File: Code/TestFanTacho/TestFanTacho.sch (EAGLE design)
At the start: 10 parts, among them IC1 317T, T1 BC548

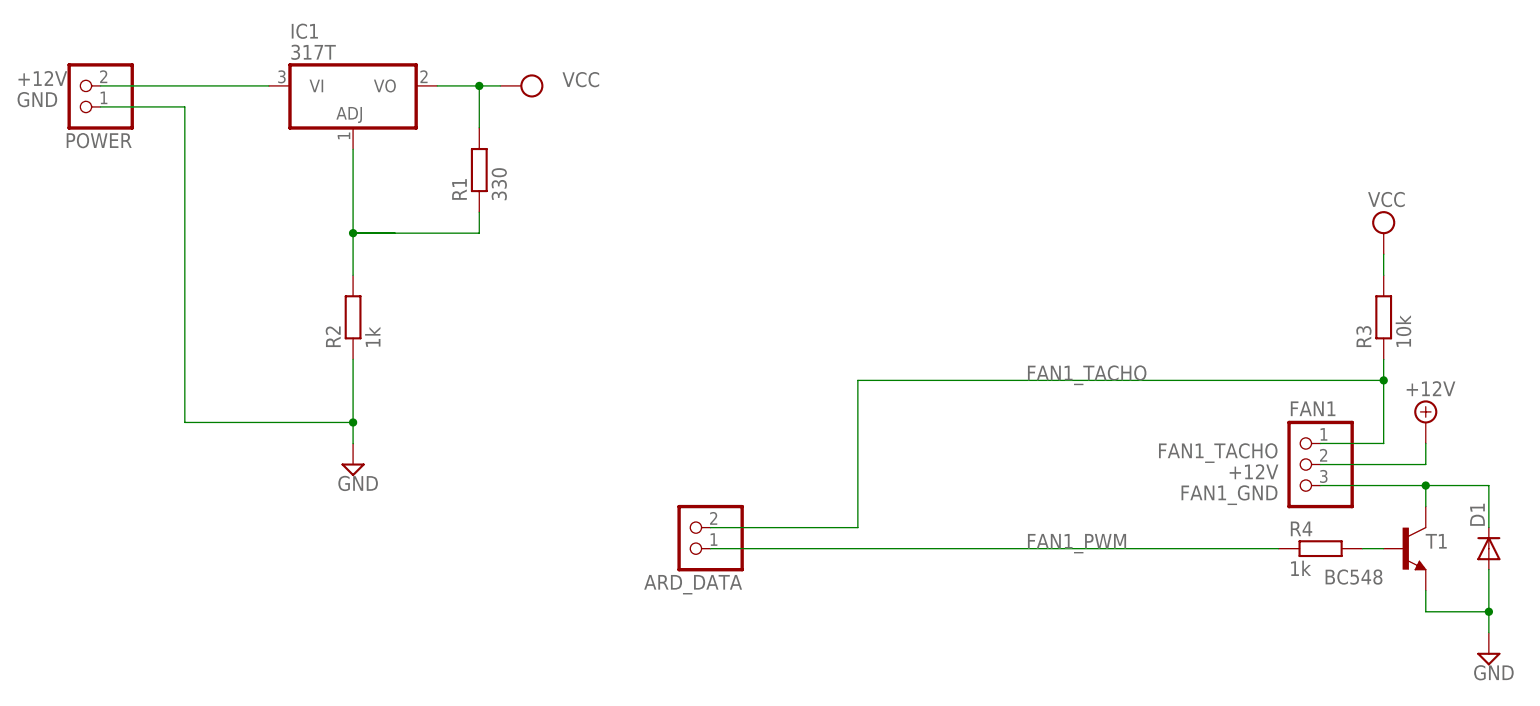
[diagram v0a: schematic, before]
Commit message: Added test for the fan tacho
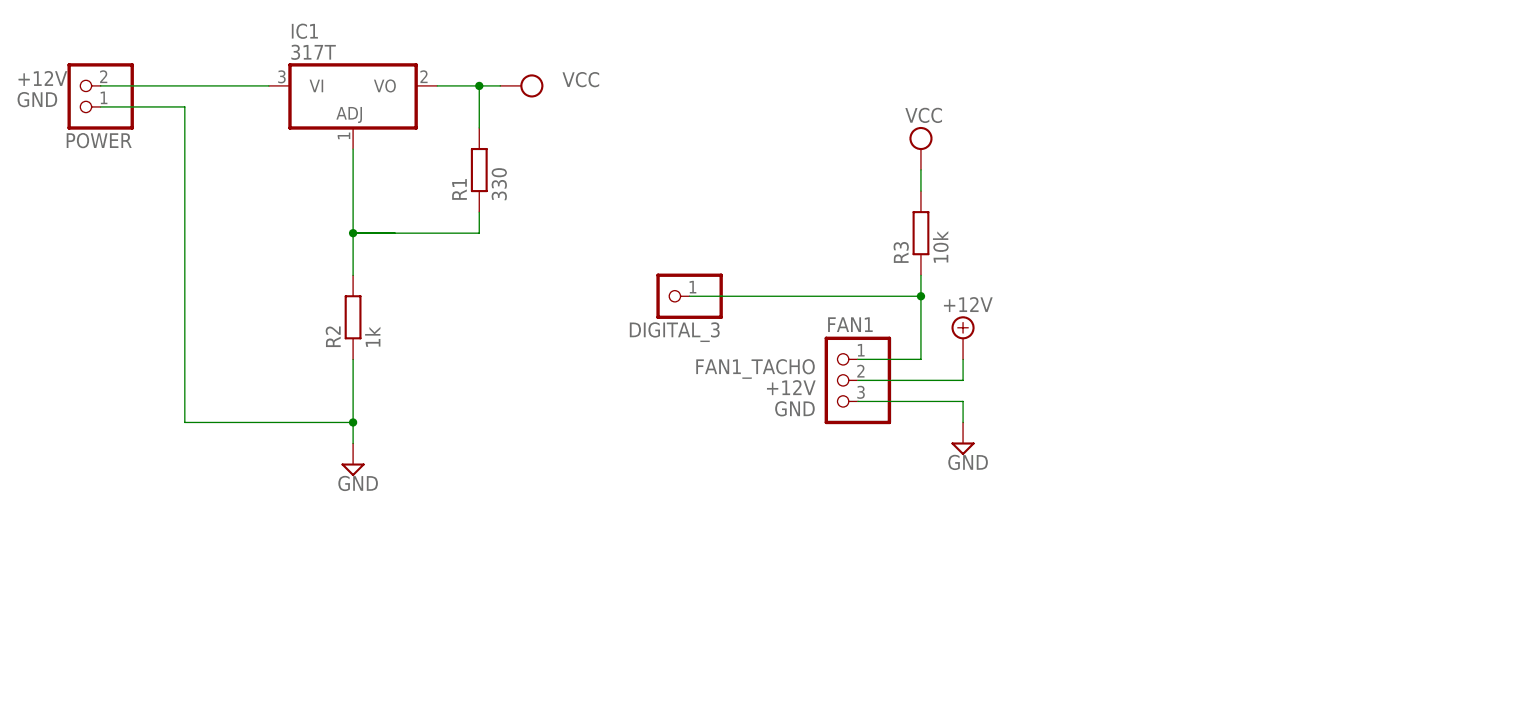
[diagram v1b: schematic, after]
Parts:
- removed ARD_DATA: (no value), EnigmaMon:PINHD-1X2
- removed D1: (no value), diode:DIODE-D-7.5
- removed R4: 1k, rcl:R-EU_0204/7
- removed T1: BC548, transistor:BC547
- added DIGITAL_3: (no value), pinhead:PINHD-1X1
- R2: device EnigmaMon:R-EU_0207/7 -> rcl:R-EU_0207/12
- R3: device rcl:R-EU_0207/10 -> rcl:R-EU_0207/7
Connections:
- removed net FAN1_GND: D1.C, FAN1.3, T1.C
- removed net FAN1_PWM: ARD_DATA.1, R4.1
- removed net N$2: R4.2, T1.B
- net FAN1_TACHO: now also DIGITAL_3.1; no longer ARD_DATA.2
- net GND: now also FAN1.3; no longer D1.A, T1.E
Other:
- moved on the sheet: FAN1, R3
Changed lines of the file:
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@@
 <parts>
 <part name="FAN1" library="pinhead" deviceset="PINHD-1X3" device=""/>
-<part name="T1" library="transistor" deviceset="BC547" device="" value="BC548"/>
-<part name="SUPPLY12" library="EnigmaMon" deviceset="GND" device=""/>
 <part name="SUPPLY13" library="EnigmaMon" deviceset="+12V" device=""/>
-<part name="D1" library="diode" deviceset="DIODE-" device="D-7.5"/>
-<part name="R4" library="rcl" deviceset="R-EU_" device="0204/7" value="1k"/>
-<part name="R3" library="rcl" deviceset="R-EU_" device="0207/10" value="10k"/>
+<part name="R3" library="rcl" deviceset="R-EU_" device="0207/7" value="10k"/>
 <part name="SUPPLY1" library="supply2" deviceset="VCC" device=""/>
-<part name="ARD_DATA" library="EnigmaMon" deviceset="PINHD-1X2" device=""/>
 <part name="IC1" library="Rodentometer" deviceset="*317" device="T"/>
 <part name="SUPPLY4" library="Rodentometer" deviceset="GND" device=""/>
@@
 <part name="SUPPLY5" library="supply2" deviceset="VCC" device=""/>
 <part name="R1" library="EnigmaMon" deviceset="R-EU_" device="0207/2V" value="330"/>
-<part name="R2" library="EnigmaMon" deviceset="R-EU_" device="0207/7" value="1k"/>
+<part name="R2" library="rcl" deviceset="R-EU_" device="0207/12" value="1k"/>
+<part name="DIGITAL_3" library="pinhead" deviceset="PINHD-1X1" device=""/>
+<part name="SUPPLY2" library="Rodentometer" deviceset="GND" device=""/>
 </parts>
 <sheets>
@@
 </plain>
 <instances>
-<instance part="FAN1" gate="A" x="78.74" y="55.88" smashed="yes" rot="MR0">
-<attribute name="VALUE" x="80.01" y="48.26" size="1.778" layer="96" rot="MR0"/>
-<attribute name="NAME" x="77.47" y="61.722" size="1.778" layer="95"/>
+<instance part="FAN1" gate="A" x="22.86" y="66.04" smashed="yes" rot="MR0">
+<attribute name="VALUE" x="24.13" y="58.42" size="1.778" layer="96" rot="MR0"/>
+<attribute name="NAME" x="21.59" y="71.882" size="1.778" layer="95"/>
 </instance>
-<instance part="T1" gate="G$1" x="91.44" y="45.72" smashed="yes">
-<attribute name="NAME" x="93.98" y="45.72" size="1.778" layer="95"/>
-<attribute name="VALUE" x="88.9" y="43.18" size="1.778" layer="96" rot="R180"/>
-</instance>
-<instance part="SUPPLY12" gate="GND" x="101.6" y="33.02"/>
-<instance part="SUPPLY13" gate="+12V" x="93.98" y="60.96"/>
-<instance part="D1" gate="G$1" x="101.6" y="45.72" rot="R90"/>
-<instance part="R4" gate="G$1" x="81.28" y="45.72"/>
-<instance part="R3" gate="G$1" x="88.9" y="73.66" rot="R90"/>
-<instance part="SUPPLY1" gate="G$1" x="88.9" y="83.82"/>
-<instance part="ARD_DATA" gate="G$1" x="5.08" y="48.26" rot="R180"/>
+<instance part="SUPPLY13" gate="+12V" x="38.1" y="71.12"/>
+<instance part="R3" gate="G$1" x="33.02" y="83.82" rot="R90"/>
+<instance part="SUPPLY1" gate="G$1" x="33.02" y="93.98"/>
 <instance part="IC1" gate="A1" x="-35.56" y="99.06"/>
 <instance part="SUPPLY4" gate="GND" x="-35.56" y="55.88"/>
@@
 <instance part="R1" gate="G$1" x="-20.32" y="91.44" rot="R90"/>
 <instance part="R2" gate="G$1" x="-35.56" y="73.66" rot="R90"/>
+<instance part="DIGITAL_3" gate="G$1" x="2.54" y="76.2" rot="R180"/>
+<instance part="SUPPLY2" gate="GND" x="38.1" y="58.42"/>
 </instances>
 <busses>
@@
 <segment>
 <pinref part="FAN1" gate="A" pin="2"/>
-<wire x1="81.28" y1="55.88" x2="93.98" y2="55.88" width="0.1524" layer="91"/>
+<wire x1="25.4" y1="66.04" x2="38.1" y2="66.04" width="0.1524" layer="91"/>
 <pinref part="SUPPLY13" gate="+12V" pin="+12V"/>
-<wire x1="93.98" y1="55.88" x2="93.98" y2="58.42" width="0.1524" layer="91"/>
-<label x="76.2" y="55.88" size="1.778" layer="95" rot="R180"/>
+<wire x1="38.1" y1="66.04" x2="38.1" y2="68.58" width="0.1524" layer="91"/>
+<label x="20.32" y="66.04" size="1.778" layer="95" rot="R180"/>
 </segment>
 <segment>
@@
 </net>
 <net name="GND" class="0">
-<segment>
-<pinref part="SUPPLY12" gate="GND" pin="GND"/>
-<junction x="101.6" y="38.1"/>
-<wire x1="101.6" y1="38.1" x2="101.6" y2="35.56" width="0.1524" layer="91"/>
-<pinref part="D1" gate="G$1" pin="A"/>
-<wire x1="101.6" y1="43.18" x2="101.6" y2="38.1" width="0.1524" layer="91"/>
-<pinref part="T1" gate="G$1" pin="E"/>
-<wire x1="93.98" y1="40.64" x2="93.98" y2="38.1" width="0.1524" layer="91"/>
-<wire x1="101.6" y1="38.1" x2="93.98" y2="38.1" width="0.1524" layer="91"/>
-</segment>
 <segment>
 <pinref part="SUPPLY4" gate="GND" pin="GND"/>
@@
 <junction x="-35.56" y="60.96"/>
 </segment>
+<segment>
+<wire x1="25.4" y1="63.5" x2="38.1" y2="63.5" width="0.1524" layer="91"/>
+<wire x1="38.1" y1="63.5" x2="38.1" y2="60.96" width="0.1524" layer="91"/>
+<pinref part="FAN1" gate="A" pin="3"/>
+<label x="20.32" y="63.5" size="1.778" layer="95" rot="R180"/>
+<pinref part="SUPPLY2" gate="GND" pin="GND"/>
+</segment>
 </net>
 <net name="FAN1_TACHO" class="0">
 <segment>
-<wire x1="88.9" y1="66.04" x2="25.4" y2="66.04" width="0.1524" layer="91"/>
-<wire x1="88.9" y1="58.42" x2="88.9" y2="66.04" width="0.1524" layer="91"/>
-<wire x1="81.28" y1="58.42" x2="88.9" y2="58.42" width="0.1524" layer="91"/>
+<wire x1="33.02" y1="76.2" x2="5.08" y2="76.2" width="0.1524" layer="91"/>
+<wire x1="33.02" y1="68.58" x2="33.02" y2="76.2" width="0.1524" layer="91"/>
+<wire x1="25.4" y1="68.58" x2="33.02" y2="68.58" width="0.1524" layer="91"/>
 <pinref part="FAN1" gate="A" pin="1"/>
-<label x="76.2" y="58.42" size="1.778" layer="95" rot="R180"/>
-<junction x="88.9" y="66.04"/>
-<label x="45.72" y="66.04" size="1.778" layer="95"/>
+<label x="20.32" y="68.58" size="1.778" layer="95" rot="R180"/>
+<junction x="33.02" y="76.2"/>
 <pinref part="R3" gate="G$1" pin="1"/>
-<wire x1="88.9" y1="68.58" x2="88.9" y2="66.04" width="0.1524" layer="91"/>
-<wire x1="25.4" y1="66.04" x2="25.4" y2="48.26" width="0.1524" layer="91"/>
-<wire x1="25.4" y1="48.26" x2="7.62" y2="48.26" width="0.1524" layer="91"/>
-<pinref part="ARD_DATA" gate="G$1" pin="2"/>
-</segment>
-</net>
-<net name="FAN1_GND" class="0">
-<segment>
-<wire x1="81.28" y1="53.34" x2="93.98" y2="53.34" width="0.1524" layer="91"/>
-<wire x1="93.98" y1="53.34" x2="93.98" y2="50.8" width="0.1524" layer="91"/>
-<pinref part="FAN1" gate="A" pin="3"/>
-<pinref part="T1" gate="G$1" pin="C"/>
-<label x="76.2" y="53.34" size="1.778" layer="95" rot="R180"/>
-<pinref part="D1" gate="G$1" pin="C"/>
-<wire x1="93.98" y1="53.34" x2="101.6" y2="53.34" width="0.1524" layer="91"/>
-<wire x1="101.6" y1="53.34" x2="101.6" y2="48.26" width="0.1524" layer="91"/>
-<junction x="93.98" y="53.34"/>
-</segment>
-</net>
-<net name="FAN1_PWM" class="0">
-<segment>
-<pinref part="R4" gate="G$1" pin="1"/>
-<label x="45.72" y="45.72" size="1.778" layer="95"/>
-<wire x1="76.2" y1="45.72" x2="7.62" y2="45.72" width="0.1524" layer="91"/>
-<pinref part="ARD_DATA" gate="G$1" pin="1"/>
-</segment>
-</net>
-<net name="N$2" class="0">
-<segment>
-<pinref part="T1" gate="G$1" pin="B"/>
-<wire x1="88.9" y1="45.72" x2="86.36" y2="45.72" width="0.1524" layer="91"/>
-<pinref part="R4" gate="G$1" pin="2"/>
+<wire x1="33.02" y1="78.74" x2="33.02" y2="76.2" width="0.1524" layer="91"/>
+<pinref part="DIGITAL_3" gate="G$1" pin="1"/>
 </segment>
 </net>
@@
 <segment>
 <pinref part="R3" gate="G$1" pin="2"/>
-<wire x1="88.9" y1="78.74" x2="88.9" y2="81.28" width="0.1524" layer="91"/>
+<wire x1="33.02" y1="88.9" x2="33.02" y2="91.44" width="0.1524" layer="91"/>
 <pinref part="SUPPLY1" gate="G$1" pin="VCC"/>
 </segment>
